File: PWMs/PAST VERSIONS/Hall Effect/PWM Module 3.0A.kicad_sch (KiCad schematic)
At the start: 6 parts, among them J1 PH1-20-UA, J2 Conn_01x02_Pin, J3 Conn_01x02_Pin, J4 PH1-20-UA, K1 G2RL-1A-E, K2 G2RL-1A-E

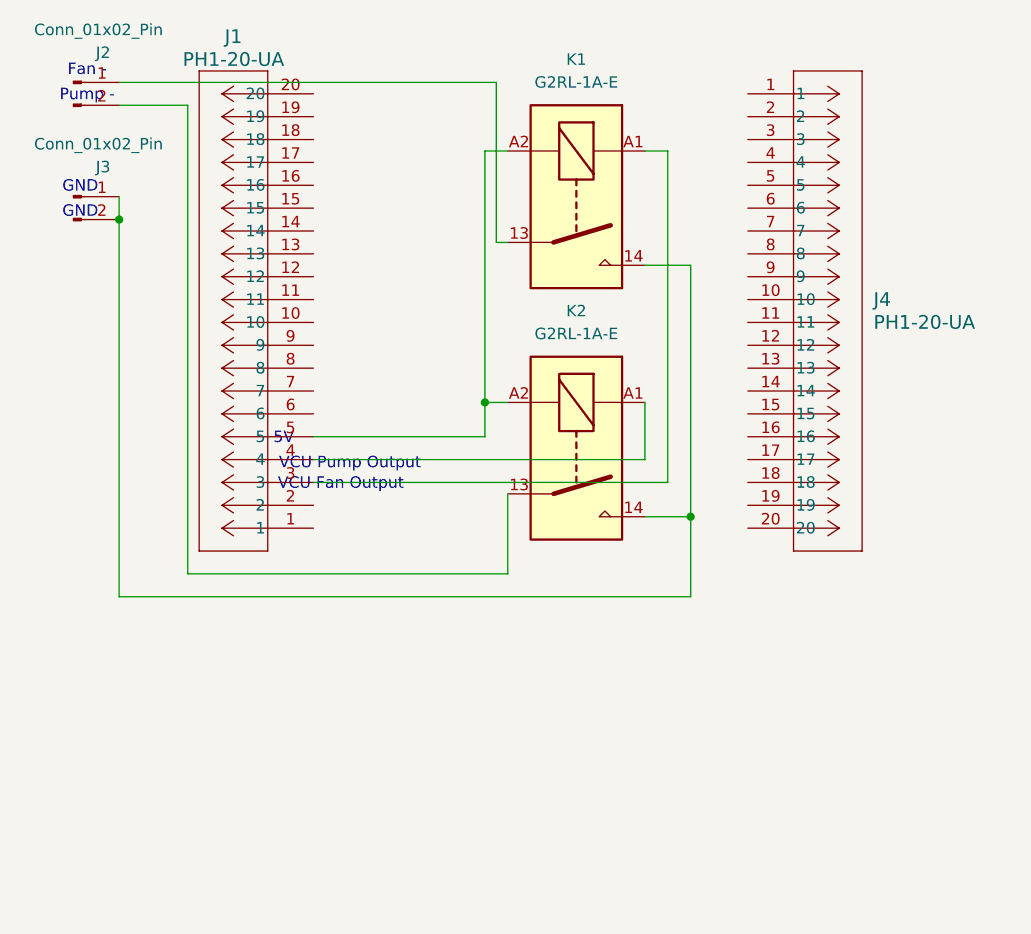
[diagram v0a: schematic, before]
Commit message: Hall Effect
Added Hall Effect Circuit Files
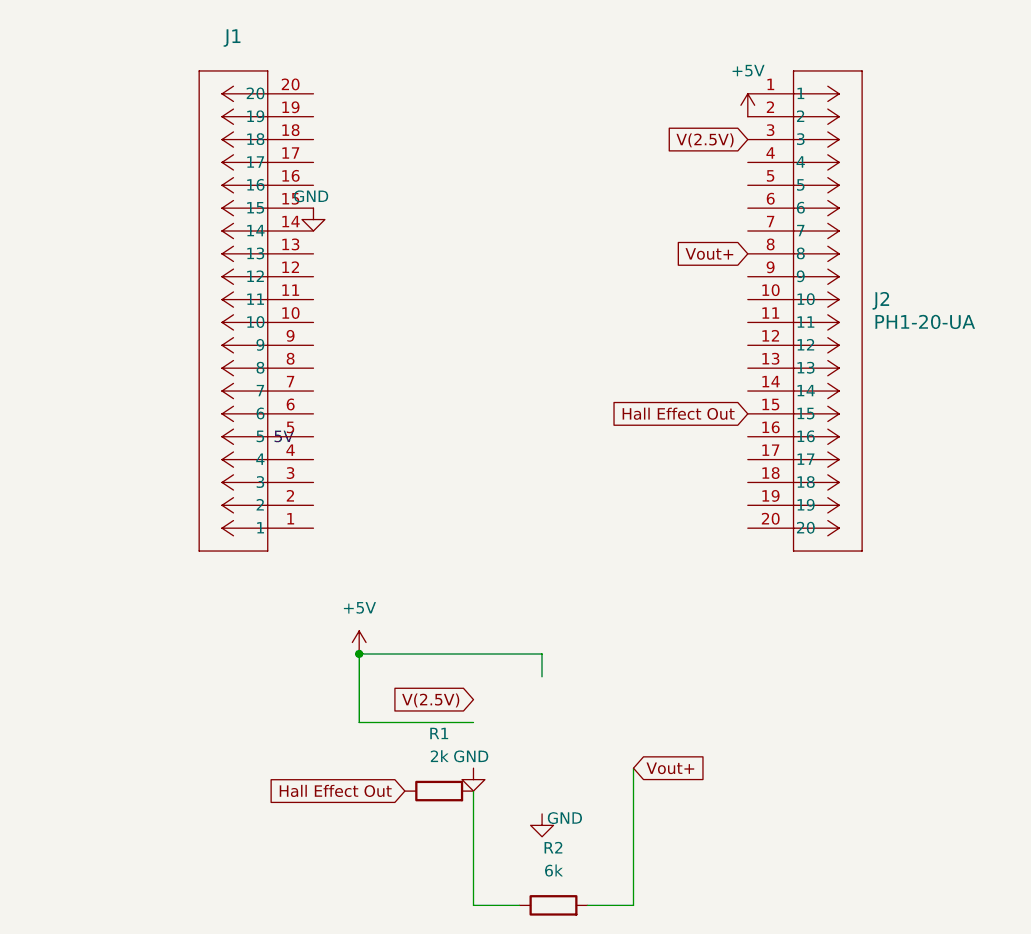
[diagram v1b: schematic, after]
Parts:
- removed J2, J3: Conn_01x02_Pin, TerminalBlock_Phoenix:TerminalBlock_Phoenix_PT-1,5-2-5.0-H_1x02_P5.00mm_Horizontal, symbol Connector:Conn_01x02_Pin
- removed K1, K2: G2RL-1A-E, Relay_THT:Relay_SPST_Omron_G2RL-1A-E, symbol Relay:G2RL-1A-E
- added R1: 2k, Resistor_THT:R_Axial_DIN0207_L6.3mm_D2.5mm_P10.16mm_Horizontal, symbol Device:R
- added R2: 6k, Resistor_THT:R_Axial_DIN0207_L6.3mm_D2.5mm_P10.16mm_Horizontal, symbol Device:R
- renumbered J4 to J2
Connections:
- net GND: now reaches J1.15
- net Hall Effect Out: now reaches J2.15
- net Hall Effect Out: now also R1.1
- net +5V: now reaches J2.2
- net V(2.5V): now reaches J2.3
- net Vout+: now reaches J2.8
- net Vout+: now also R2.2
- new net: R1.2, R2.1
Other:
- note removed: "Fan -"
- note removed: "GND"
- note removed: "Pump -"
- note removed: "VCU Fan Output"
- note removed: "VCU Pump Output"
